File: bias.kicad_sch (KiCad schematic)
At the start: 20 parts, among them Q2001 DPLS350E, Q2002 DNLS350E, Q2003 DPLS350E, Q2004 DPLS350E, Q2005 DNLS350E, Q2006 DNLS350E, Q2007 TIP41C, Q2008 TIP42C

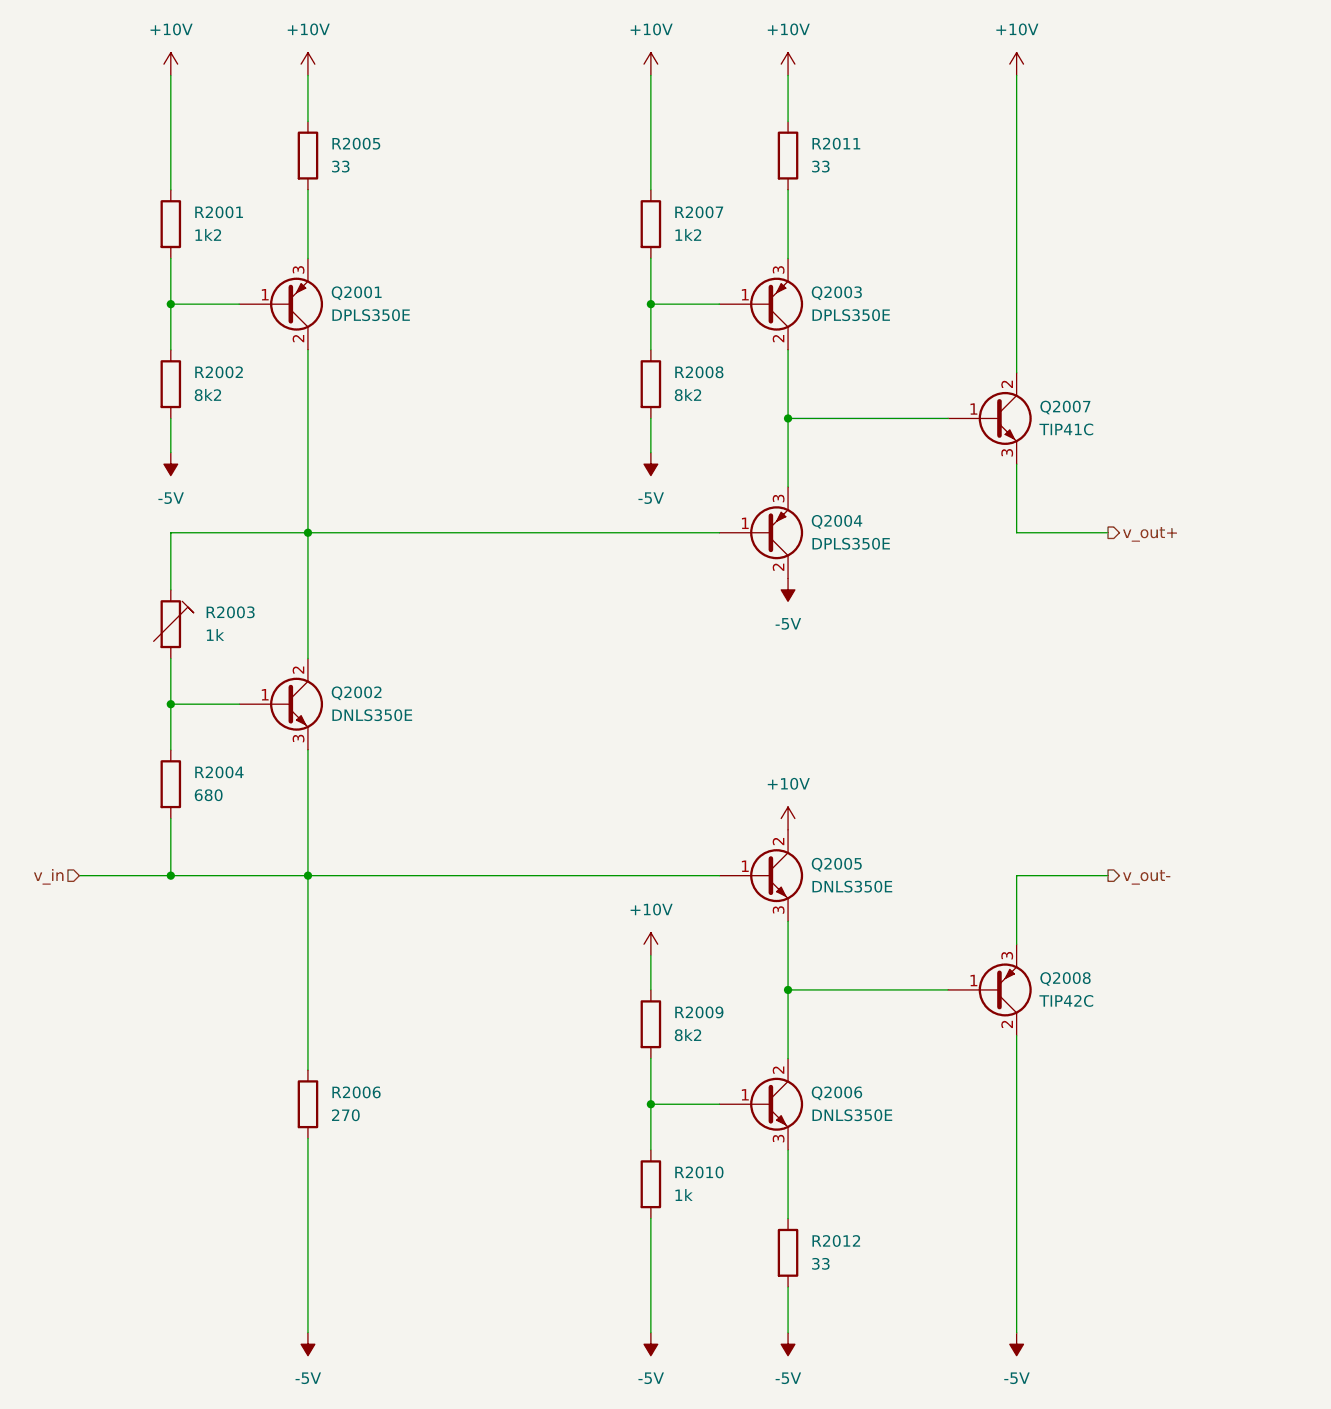
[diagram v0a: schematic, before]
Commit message: change rubber diode vbe multiplier trimmer position
changed position prohibits excess dropoff voltage in case of machanical failure of trimmer
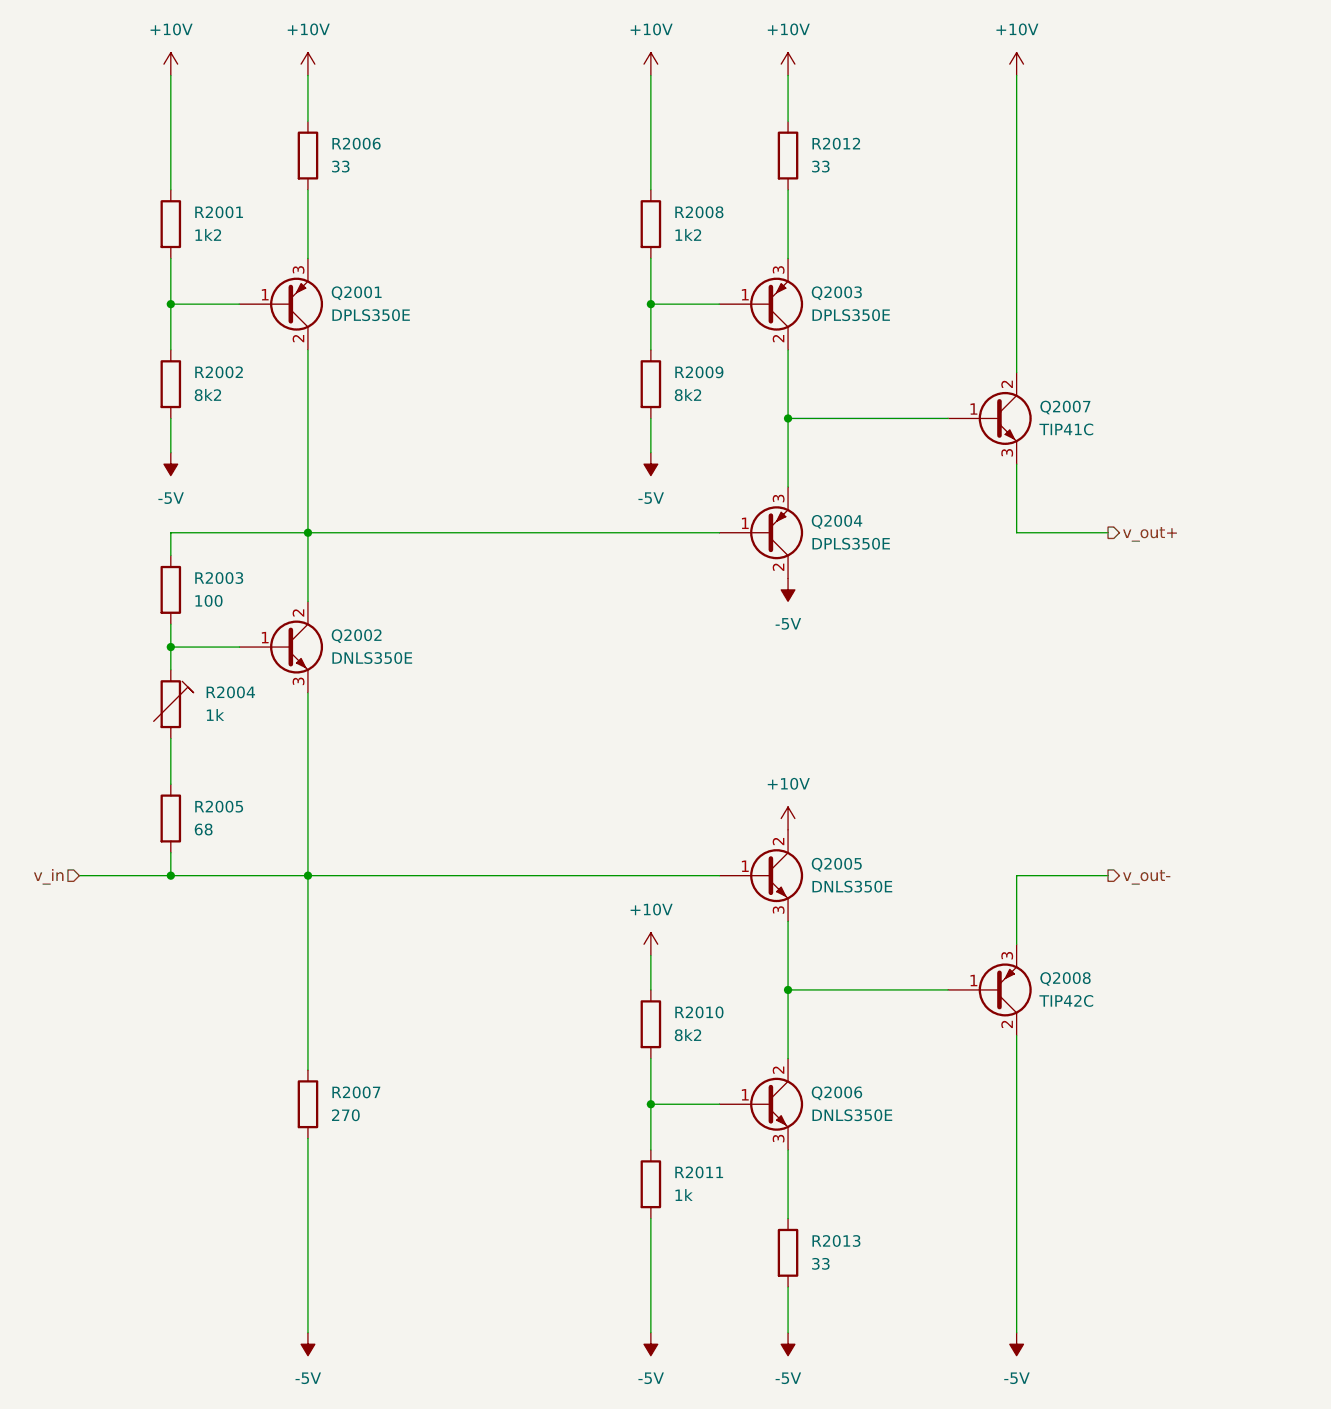
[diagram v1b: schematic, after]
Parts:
- added R2003: 100, symbol Device:R
- R2005: renamed from R2004; value 680 -> 68
- renumbered R2003 to R2004, R2005 to R2006, R2006 to R2007, R2007 to R2008, R2008 to R2009, R2009 to R2010, R2010 to R2011, R2011 to R2012, R2012 to R2013
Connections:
- net at R2004.2, R2005.1: no longer Q2002.1 (B)
- net at Q2001.2 (C), Q2002.2 (C), Q2004.1 (B): now also R2003.1; no longer R2004.1
- new net: Q2002.1 (B), R2003.2, R2004.1
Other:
- moved on the sheet: Q2002, R2004, R2005

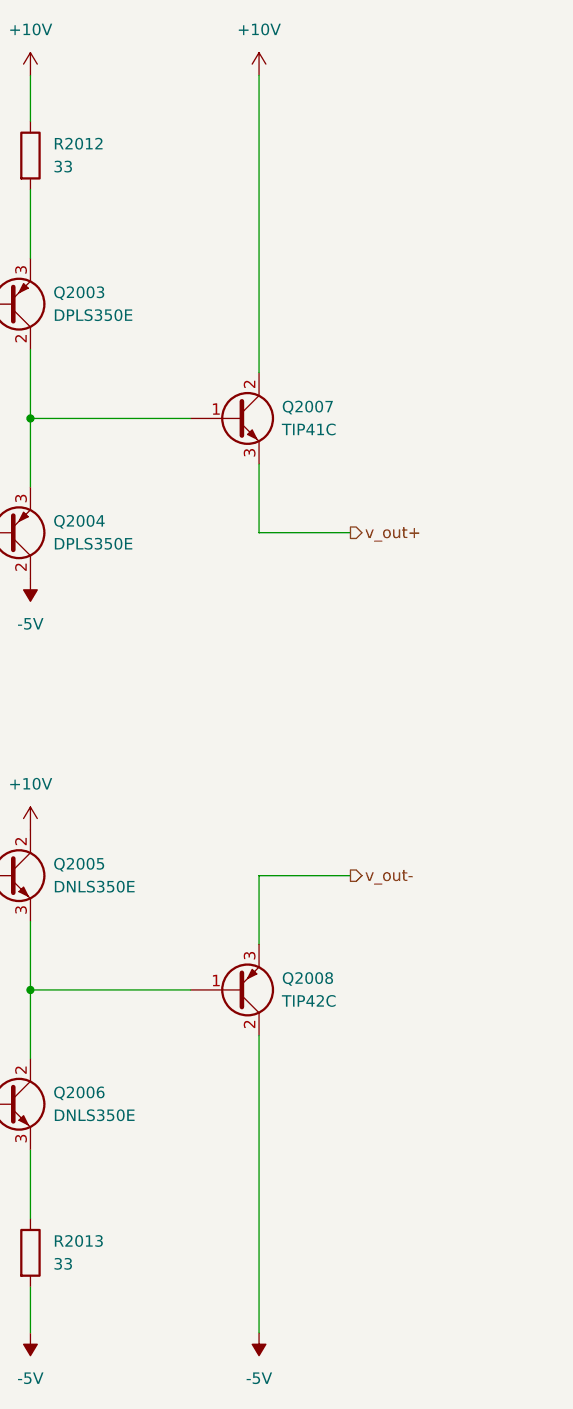
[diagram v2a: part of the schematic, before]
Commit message: add heatsinks, thermal pads, mounting clips
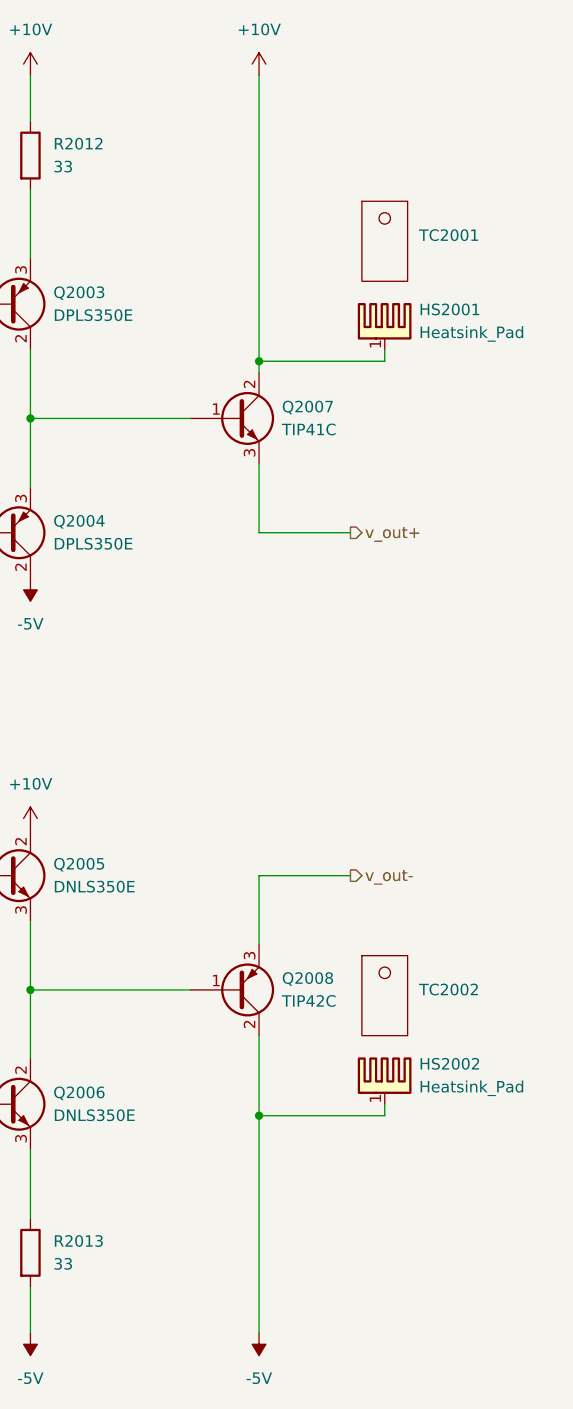
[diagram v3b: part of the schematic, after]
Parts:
- added HS2001, HS2002: Heatsink_Pad, symbol Mechanical:Heatsink_Pad
- added TC2001, TC2002: ~, symbol pss:Thermal_Conductor
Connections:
- net +10V: now also HS2001.1
- net -5V: now also HS2002.1
